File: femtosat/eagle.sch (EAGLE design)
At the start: 15 parts, among them U1 ATMEGA328P_TQFP, U2 915MHz, U3 3.3V/150mA, Y1 16MHz

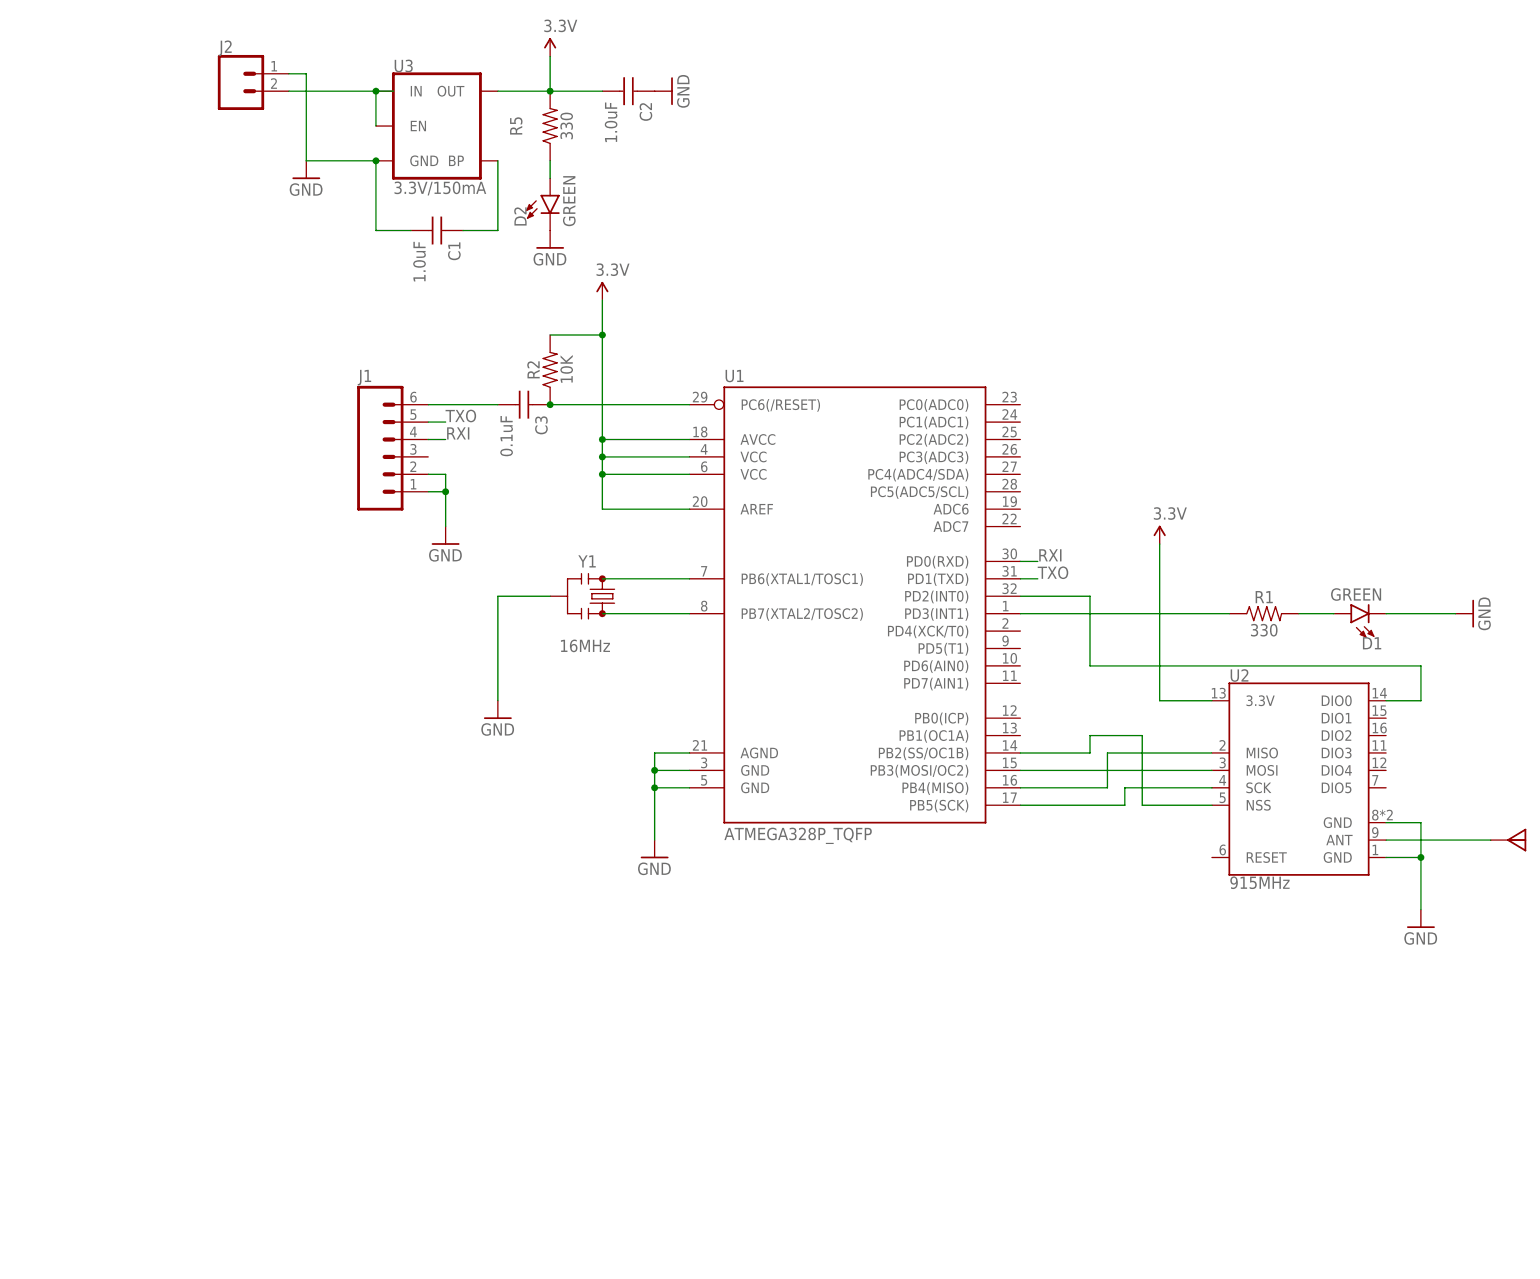
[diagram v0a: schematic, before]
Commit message: Started Sensor connections
Started connecting the sensors though I don't know where all the pins should connect.
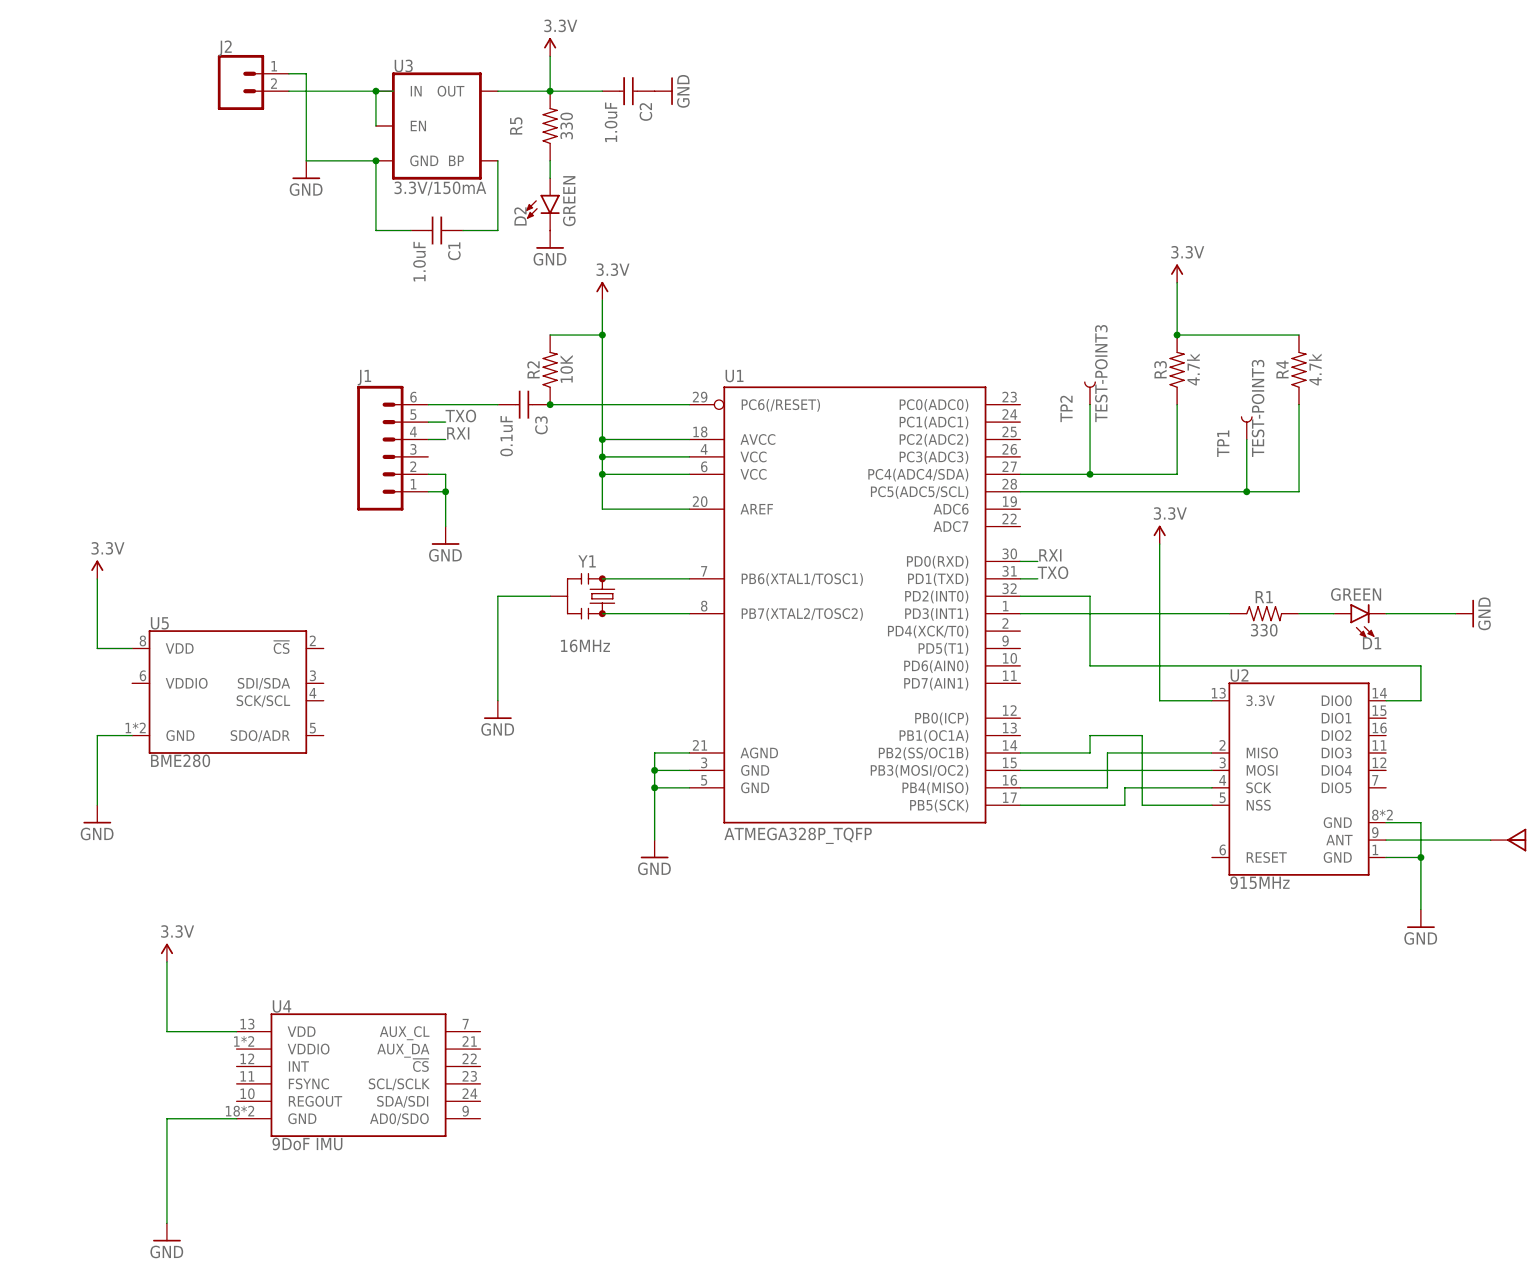
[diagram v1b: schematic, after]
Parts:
- added R3, R4: 4.7k, femtosat:RESISTOR_4.7KOHM-0603-1/10W-1%
- added TP1, TP2: TEST-POINT3, femtosat:TEST-POINT3
- added U4: 9DoF IMU, femtosat:MPU9250
- added U5: BME280, femtosat:BME280
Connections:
- new net N$22: R3.1, TP2.1, U1.PC4(ADC4/SDA)
- new net N$23: R4.1, TP1.1, U1.PC5(ADC5/SCL)
- net 3.3V: now also R3.2, R4.2, U4.VDD, U5.VDD
- net GND: now also U4.GND, U5.GND
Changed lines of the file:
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@@
 <part name="C3" library="femtosat" deviceset="CAPACITOR_0.1UF" device="" value="0.1uF"/>
 <part name="GND8" library="femtosat" deviceset="GND" device=""/>
+<part name="U4" library="femtosat" deviceset="MPU9250" device="" value="9DoF IMU"/>
+<part name="GND9" library="femtosat" deviceset="GND" device=""/>
+<part name="P+4" library="femtosat" deviceset="3.3V" device=""/>
+<part name="U5" library="femtosat" deviceset="BME280" device="" value="BME280"/>
+<part name="GND10" library="femtosat" deviceset="GND" device=""/>
+<part name="P+5" library="femtosat" deviceset="3.3V" device=""/>
+<part name="R3" library="femtosat" deviceset="RESISTOR_4.7KOHM" device="-0603-1/10W-1%" value="4.7k"/>
+<part name="R4" library="femtosat" deviceset="RESISTOR_4.7KOHM" device="-0603-1/10W-1%" value="4.7k"/>
+<part name="P+6" library="femtosat" deviceset="3.3V" device=""/>
+<part name="TP1" library="femtosat" deviceset="TEST-POINT" device="3"/>
+<part name="TP2" library="femtosat" deviceset="TEST-POINT" device="3"/>
 </parts>
 <sheets>
@@
 <instance part="GND8" gate="1" x="71.12" y="119.38" smashed="yes">
 <attribute name="VALUE" x="68.58" y="116.84" size="1.778" layer="96"/>
+</instance>
+<instance part="U4" gate="G$1" x="58.42" y="40.64" smashed="yes">
+<attribute name="NAME" x="45.72" y="51.054" size="1.778" layer="95" font="vector"/>
+<attribute name="VALUE" x="45.72" y="32.766" size="1.778" layer="96" font="vector" align="top-left"/>
+</instance>
+<instance part="GND9" gate="1" x="30.48" y="17.78" smashed="yes">
+<attribute name="VALUE" x="27.94" y="15.24" size="1.778" layer="96"/>
+</instance>
+<instance part="P+4" gate="G$1" x="30.48" y="58.42" smashed="yes">
+<attribute name="VALUE" x="29.464" y="61.976" size="1.778" layer="96"/>
+</instance>
+<instance part="U5" gate="U1" x="38.1" y="99.06" smashed="yes">
+<attribute name="NAME" x="27.94" y="106.934" size="1.778" layer="95"/>
+<attribute name="VALUE" x="27.94" y="88.646" size="1.778" layer="95" align="top-left"/>
+</instance>
+<instance part="GND10" gate="1" x="20.32" y="78.74" smashed="yes">
+<attribute name="VALUE" x="17.78" y="76.2" size="1.778" layer="96"/>
+</instance>
+<instance part="P+5" gate="G$1" x="20.32" y="114.3" smashed="yes">
+<attribute name="VALUE" x="19.304" y="117.856" size="1.778" layer="96"/>
+</instance>
+<instance part="R3" gate="G$1" x="177.8" y="144.78" smashed="yes" rot="R90">
+<attribute name="NAME" x="176.276" y="144.78" size="1.778" layer="95" font="vector" rot="R90" align="bottom-center"/>
+<attribute name="VALUE" x="179.324" y="144.78" size="1.778" layer="96" font="vector" rot="R90" align="top-center"/>
+</instance>
+<instance part="R4" gate="G$1" x="195.58" y="144.78" smashed="yes" rot="R90">
+<attribute name="NAME" x="194.056" y="144.78" size="1.778" layer="95" font="vector" rot="R90" align="bottom-center"/>
+<attribute name="VALUE" x="197.104" y="144.78" size="1.778" layer="96" font="vector" rot="R90" align="top-center"/>
+</instance>
+<instance part="P+6" gate="G$1" x="177.8" y="157.48" smashed="yes">
+<attribute name="VALUE" x="176.784" y="161.036" size="1.778" layer="96"/>
+</instance>
+<instance part="TP1" gate="G$1" x="187.96" y="134.62" smashed="yes" rot="R90">
+<attribute name="NAME" x="185.42" y="132.08" size="1.778" layer="95" font="vector" rot="R90"/>
+<attribute name="VALUE" x="190.5" y="132.08" size="1.778" layer="96" font="vector" rot="R90"/>
+</instance>
+<instance part="TP2" gate="G$1" x="165.1" y="139.7" smashed="yes" rot="R90">
+<attribute name="NAME" x="162.56" y="137.16" size="1.778" layer="95" font="vector" rot="R90"/>
+<attribute name="VALUE" x="167.64" y="137.16" size="1.778" layer="96" font="vector" rot="R90"/>
 </instance>
 </instances>
@@
 <junction x="71.12" y="127"/>
 <pinref part="GND8" gate="1" pin="GND"/>
+</segment>
+<segment>
+<pinref part="U4" gate="G$1" pin="GND"/>
+<wire x1="40.64" y1="35.56" x2="30.48" y2="35.56" width="0.1524" layer="91"/>
+<wire x1="30.48" y1="35.56" x2="30.48" y2="20.32" width="0.1524" layer="91"/>
+<pinref part="GND9" gate="1" pin="GND"/>
+</segment>
+<segment>
+<pinref part="U5" gate="U1" pin="GND"/>
+<wire x1="25.4" y1="91.44" x2="20.32" y2="91.44" width="0.1524" layer="91"/>
+<wire x1="20.32" y1="91.44" x2="20.32" y2="81.28" width="0.1524" layer="91"/>
+<pinref part="GND10" gate="1" pin="GND"/>
 </segment>
 </net>
@@
 <pinref part="C2" gate="G$1" pin="2"/>
 </segment>
+<segment>
+<pinref part="U4" gate="G$1" pin="VDD"/>
+<wire x1="40.64" y1="48.26" x2="30.48" y2="48.26" width="0.1524" layer="91"/>
+<wire x1="30.48" y1="48.26" x2="30.48" y2="58.42" width="0.1524" layer="91"/>
+<pinref part="P+4" gate="G$1" pin="3.3V"/>
+</segment>
+<segment>
+<pinref part="U5" gate="U1" pin="VDD"/>
+<wire x1="25.4" y1="104.14" x2="20.32" y2="104.14" width="0.1524" layer="91"/>
+<wire x1="20.32" y1="104.14" x2="20.32" y2="114.3" width="0.1524" layer="91"/>
+<pinref part="P+5" gate="G$1" pin="3.3V"/>
+</segment>
+<segment>
+<pinref part="R3" gate="G$1" pin="2"/>
+<pinref part="R4" gate="G$1" pin="2"/>
+<wire x1="177.8" y1="149.86" x2="195.58" y2="149.86" width="0.1524" layer="91"/>
+<wire x1="177.8" y1="149.86" x2="177.8" y2="157.48" width="0.1524" layer="91"/>
+<junction x="177.8" y="149.86"/>
+<pinref part="P+6" gate="G$1" pin="3.3V"/>
+</segment>
 </net>
 <net name="N$8" class="0">
@@
 </segment>
 </net>
+<net name="N$22" class="0">
+<segment>
+<pinref part="U1" gate="U$1" pin="PC4(ADC4/SDA)"/>
+<wire x1="154.94" y1="129.54" x2="165.1" y2="129.54" width="0.1524" layer="91"/>
+<wire x1="165.1" y1="129.54" x2="177.8" y2="129.54" width="0.1524" layer="91"/>
+<wire x1="177.8" y1="129.54" x2="177.8" y2="139.7" width="0.1524" layer="91"/>
+<pinref part="R3" gate="G$1" pin="1"/>
+<pinref part="TP2" gate="G$1" pin="1"/>
+<wire x1="165.1" y1="139.7" x2="165.1" y2="129.54" width="0.1524" layer="91"/>
+<junction x="165.1" y="129.54"/>
+</segment>
+</net>
+<net name="N$23" class="0">
+<segment>
+<pinref part="U1" gate="U$1" pin="PC5(ADC5/SCL)"/>
+<wire x1="154.94" y1="127" x2="187.96" y2="127" width="0.1524" layer="91"/>
+<wire x1="187.96" y1="127" x2="195.58" y2="127" width="0.1524" layer="91"/>
+<wire x1="195.58" y1="127" x2="195.58" y2="139.7" width="0.1524" layer="91"/>
+<pinref part="R4" gate="G$1" pin="1"/>
+<pinref part="TP1" gate="G$1" pin="1"/>
+<wire x1="187.96" y1="134.62" x2="187.96" y2="127" width="0.1524" layer="91"/>
+<junction x="187.96" y="127"/>
+</segment>
+</net>
